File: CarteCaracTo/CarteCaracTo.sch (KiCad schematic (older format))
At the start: 23 parts, among them J2 Conn_01x01, J3 Conn_Coaxial, J4 Conn_Coaxial, J5 Conn_Coaxial, J50 Sub-D50_F, J51 DB15_Male_MountingHoles, J52 DB25_Female_MountingHoles, J6 Conn_Coaxial, J7 Conn_Coaxial, J8 Conn_Coaxial, SW1 SW_3PDT, SW2 SW_DIP_x05, SW3 SW_Slide_DP3T, SW4 SW_SPDT, SW5 SW_SPDT, SW6 SW_SPDT, SW7 SW_3PDT

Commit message: mineur
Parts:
- added U1: OPA4376, Package_SO:SOIC-14_3.9x8.7mm_P1.27mm, symbol Amplifier_Operational:OPA4376
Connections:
- net labels added: +12v
- wire segments 382 -> 398
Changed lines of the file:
@@
 Wire Wire Line
 	1700 10850 1700 10750
+$Comp
+L Amplifier_Operational:OPA4376 U1
+U 5 1 6238513D
+P 7100 10275
+F 0 "U1" H 7058 10321 50  0000 L CNN
+F 1 "OPA4376" H 7058 10230 50  0000 L CNN
+F 2 "Package_SO:SOIC-14_3.9x8.7mm_P1.27mm" H 7050 10375 50  0001 C CNN
+F 3 "http://www.ti.com/lit/ds/symlink/opa376.pdf" H 7150 10475 50  0001 C CNN
+	5    7100 10275
+	1    0    0    -1
+$EndComp
+$Comp
+L Amplifier_Operational:OPA4376 U1
+U 4 1 623861C7
+P 6200 10275
+F 0 "U1" H 6200 10642 50  0000 C CNN
+F 1 "OPA4376" H 6200 10551 50  0000 C CNN
+F 2 "Package_SO:SOIC-14_3.9x8.7mm_P1.27mm" H 6150 10375 50  0001 C CNN
+F 3 "http://www.ti.com/lit/ds/symlink/opa376.pdf" H 6250 10475 50  0001 C CNN
+	4    6200 10275
+	1    0    0    -1
+$EndComp
+$Comp
+L power:GND #PWR0101
+U 1 1 623980F1
+P 7000 10675
+F 0 "#PWR0101" H 7000 10425 50  0001 C CNN
+F 1 "GND" H 7005 10502 50  0000 C CNN
+F 2 "" H 7000 10675 50  0001 C CNN
+F 3 "" H 7000 10675 50  0001 C CNN
+	1    7000 10675
+	1    0    0    -1
+$EndComp
+Wire Wire Line
+	7000 10675 7000 10625
+Wire Wire Line
+	7000 9975 7000 9900
+Wire Wire Line
+	7000 9900 7100 9900
+Text Label 7100 9900 0    50   ~ 0
++12v
+Wire Wire Line
+	13575 1600 13350 1600
+Text Label 13350 1600 2    50   ~ 0
++12v
+Wire Wire Line
+	5900 10175 5550 10175
+Wire Wire Line
+	5550 10175 5550 10575
+Wire Wire Line
+	5900 10375 5775 10375
+Wire Wire Line
+	5775 10375 5775 10575
+Wire Wire Line
+	6500 10275 6525 10275
+Wire Wire Line
+	6525 10275 6525 10575
+Wire Wire Line
+	5550 10575 5775 10575
+Wire Wire Line
+	6900 10575 6900 10625
+Wire Wire Line
+	6900 10625 7000 10625
+Connection ~ 5775 10575
+Wire Wire Line
+	5775 10575 6525 10575
+Connection ~ 7000 10625
+Wire Wire Line
+	7000 10625 7000 10575
+Connection ~ 6525 10575
+Wire Wire Line
+	6525 10575 6900 10575
 $EndSCHEMATC

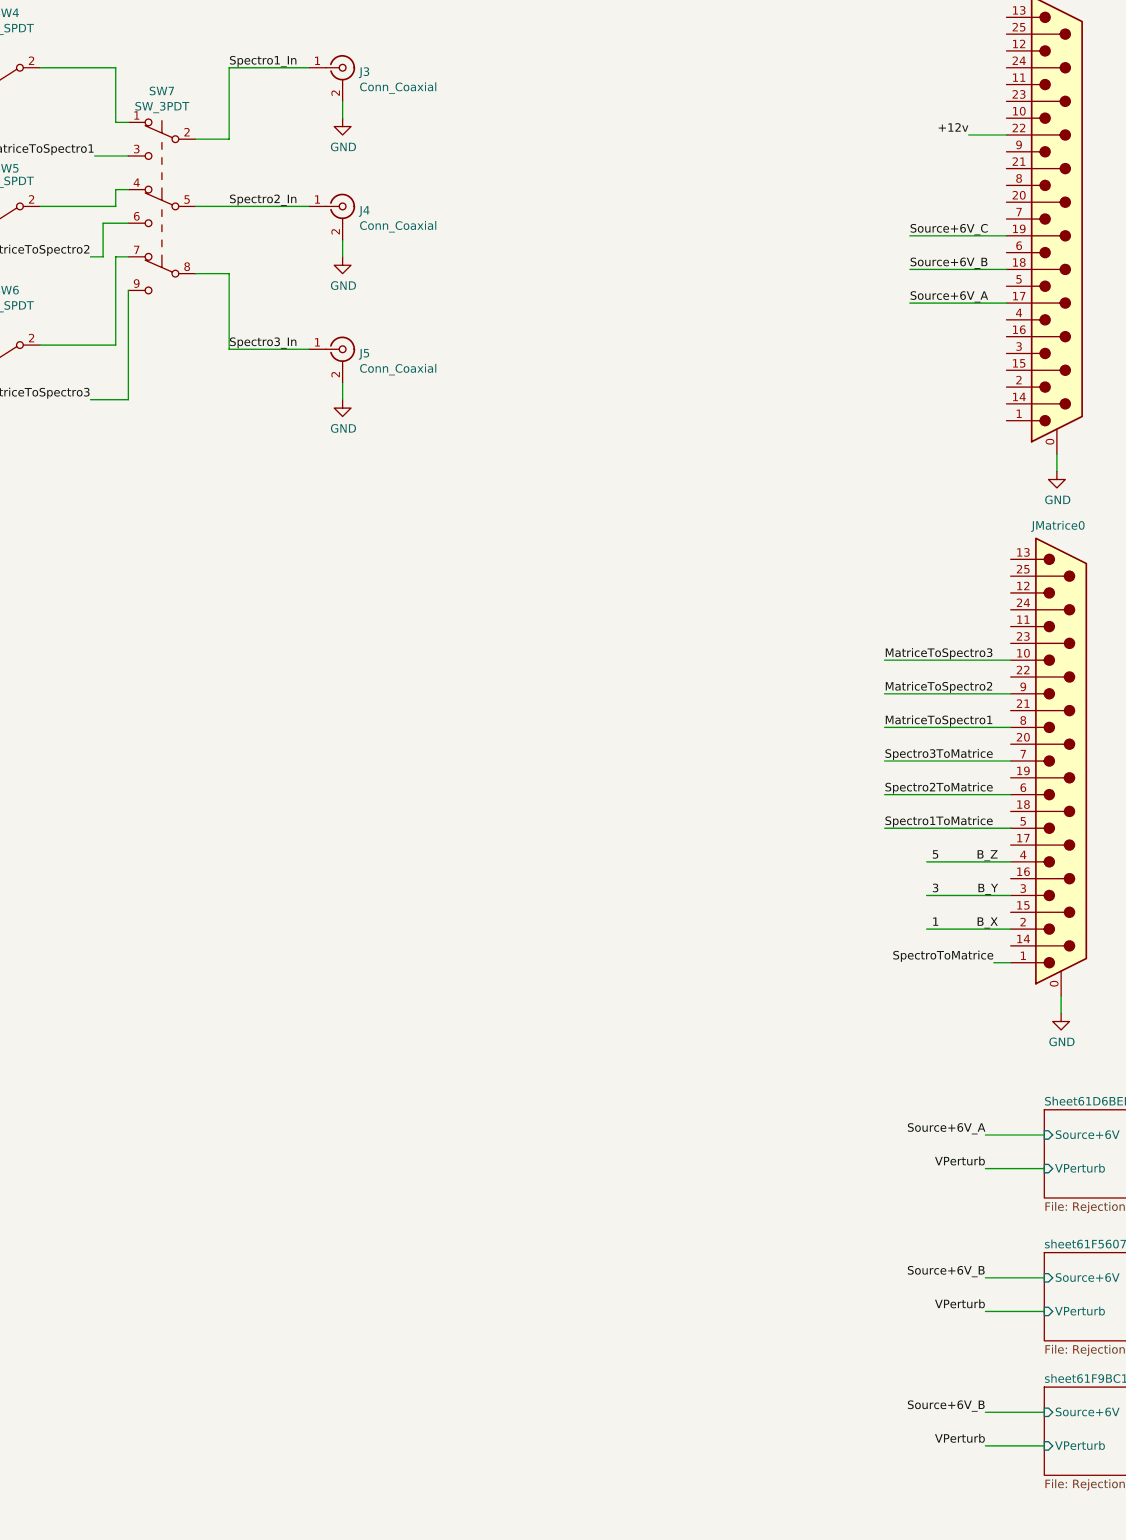
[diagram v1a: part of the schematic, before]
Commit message: Mise en forme de la carte + version carte ASIC et Carac separées
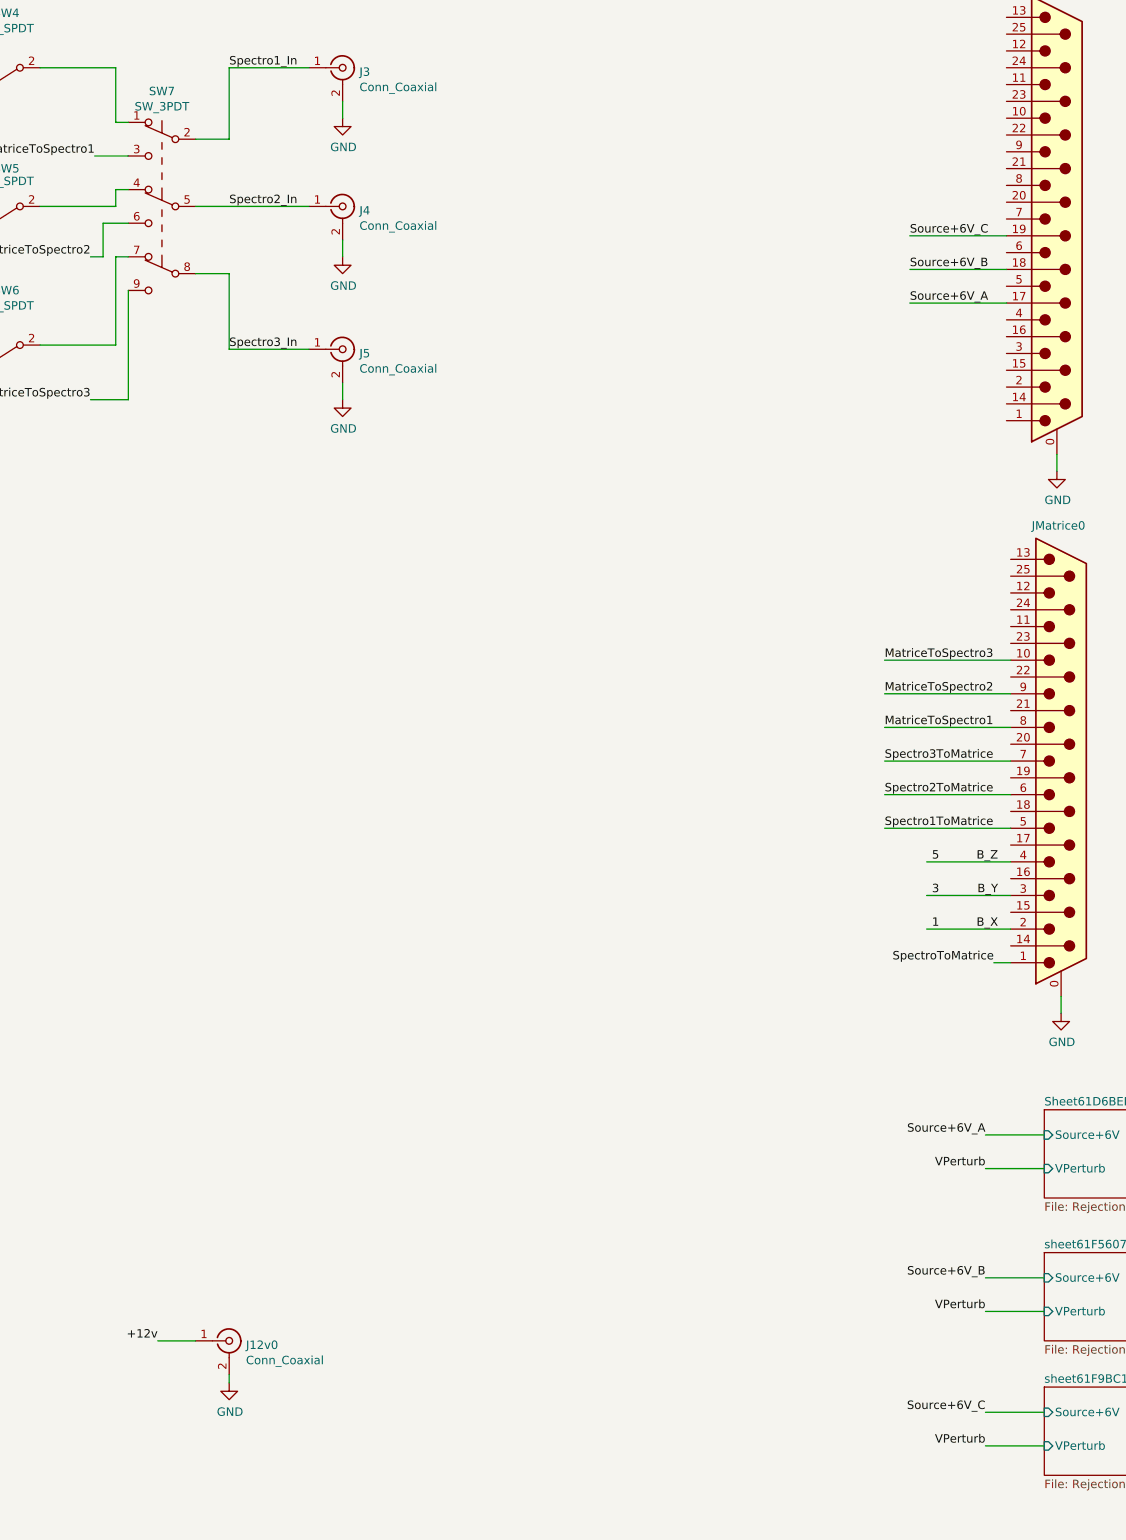
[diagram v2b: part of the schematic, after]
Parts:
- added J12v0: Conn_Coaxial, Connector_Coaxial:SMB_Jack_Vertical, symbol Connector:Conn_Coaxial
- JGSE0, JMatrice0: footprint LibPersoNadj:DCCM25PCBRPN -> Connector_Dsub:DSUB-25_Male_Horizontal_P2.77x2.84mm_EdgePinOffset9.90mm_Housed_MountingHolesOffset11.32mm
- SW7: footprint LibPersoNadj:Switch_DP3T_Slide_MHS233K -> LibPersoNadj:SW_3PDT_M2032TNW01_NKK
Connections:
- wire segments 398 -> 399
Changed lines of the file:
@@
 F 0 "JGSE0" H 13750 3500 50  0000 L CNN
 F 1 "DB25_Male_MountingHoles" H 14055 2011 50  0001 L CNN
-F 2 "LibPersoNadj:DCCM25PCBRPN" H 13875 2100 50  0001 C CNN
+F 2 "Connector_Dsub:DSUB-25_Male_Horizontal_P2.77x2.84mm_EdgePinOffset9.90mm_Housed_MountingHolesOffset11.32mm" H 13875 2100 50  0001 C CNN
 F 3 " ~" H 13875 2100 50  0001 C CNN
 	1    13875 2100
@@
 F 0 "JMatrice0" H 13725 6725 50  0000 L CNN
 F 1 "DB25_Male_MountingHoles" H 14080 5236 50  0001 L CNN
-F 2 "LibPersoNadj:DCCM25PCBRPN" H 13900 5325 50  0001 C CNN
+F 2 "Connector_Dsub:DSUB-25_Male_Horizontal_P2.77x2.84mm_EdgePinOffset9.90mm_Housed_MountingHolesOffset11.32mm" H 13900 5325 50  0001 C CNN
 F 3 " ~" H 13900 5325 50  0001 C CNN
 	1    13900 5325
@@
 F 0 "SW7" H 8550 2710 50  0000 C CNN
 F 1 "SW_3PDT" H 8550 2619 50  0000 C CNN
-F 2 "LibPersoNadj:Switch_DP3T_Slide_MHS233K" H 8550 2425 50  0001 C CNN
+F 2 "LibPersoNadj:SW_3PDT_M2032TNW01_NKK" H 8550 2425 50  0001 C CNN
 F 3 "~" H 8550 2425 50  0001 C CNN
 	1    8550 2025
@@
 	13800 9400 13450 9400
 Text Label 13450 9200 2    50   ~ 0
-Source+6V_B
+Source+6V_C
 Text Label 15125 9300 0    50   ~ 0
 +6V_B
@@
 +12v
 Wire Wire Line
-	13575 1600 13350 1600
-Text Label 13350 1600 2    50   ~ 0
+	8750 8775 8525 8775
+Text Label 8525 8775 2    50   ~ 0
 +12v
 Wire Wire Line
@@
 Wire Wire Line
 	6525 10575 6900 10575
+$Comp
+L Connector:Conn_Coaxial J12v0
+U 1 1 5E2F4810
+P 8950 8775
+F 0 "J12v0" H 9050 8750 50  0000 L CNN
+F 1 "Conn_Coaxial" H 9050 8659 50  0000 L CNN
+F 2 "Connector_Coaxial:SMB_Jack_Vertical" H 8950 8775 50  0001 C CNN
+F 3 " ~" H 8950 8775 50  0001 C CNN
+	1    8950 8775
+	1    0    0    -1
+$EndComp
+$Comp
+L power:GND #PWR0102
+U 1 1 5E3490FC
+P 8950 9025
+F 0 "#PWR0102" H 8950 8775 50  0001 C CNN
+F 1 "GND" H 8955 8852 50  0000 C CNN
+F 2 "" H 8950 9025 50  0001 C CNN
+F 3 "" H 8950 9025 50  0001 C CNN
+	1    8950 9025
+	1    0    0    -1
+$EndComp
+Wire Wire Line
+	8950 9025 8950 8975
 $EndSCHEMATC

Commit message: ID des pins, option capa sur sortie, option GND ou plan de masse sur BNC
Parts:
- removed J2: Conn_01x01, Connector_Coaxial:BNC_Amphenol_B6252HB-NPP3G-50_Horizontal, symbol Connector_Generic:Conn_01x01
- added C1, C2, C3: C, Capacitor_SMD:C_0805_2012Metric_Pad1.15x1.40mm_HandSolder, symbol Device:C
- added JDec_SA1, JDec_SA2, JDec_SA3, JGND_I_SA1, JGND_I_SA2, JGND_I_SA3, JGND_O_SA1, JGND_O_SA2, JGND_O_SA3: Conn_01x03, Connector_PinHeader_2.54mm:PinHeader_1x03_P2.54mm_Vertical, symbol Connector_Generic:Conn_01x03
- added JMasse0: Conn_01x02, Connector_PinHeader_2.54mm:PinHeader_1x02_P2.54mm_Vertical, symbol Connector_Generic:Conn_01x02
- added J_12v0, J_I_SA1, J_I_SA2, J_I_SA3, J_O_SA1, J_O_SA2, J_O_SA3, J_Perturb1: Conn_01x01, Connector_PinHeader_2.54mm:PinHeader_1x01_P2.54mm_Vertical, symbol Connector_Generic:Conn_01x01
- added J_Perturb0: Conn_Coaxial, Connector_Coaxial:BNC_Amphenol_B6252HB-NPP3G-50_Horizontal, symbol Connector:Conn_Coaxial
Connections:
- net labels added: CAL, CAL_RTN, CAL_Shield, CR_X, CR_Y, CR_Z, Chassis, GNDREF, In2P_X, In2P_Y, In2P_Z, M_X, M_Y, M_Z, PWR_Shield_A, PWR_Shield_B, PWR_Shield_C, RTN_A, RTN_B, RTN_C, RTN_Mon_A, RTN_Mon_B, Sh_X, Sh_Y, Sh_Z, Temp_Mon_A, Temp_Mon_B, VDD_X, VDD_Y, VDD_Z, V_BIAS_LNA_X, V_BIAS_LNA_Y, V_BIAS_LNA_Z, XShield, YShield, ZShield
- net labels removed: SpectroToMatrice
- wire segments 399 -> 548
- no-connect marks 1 -> 10
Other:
- moved on the sheet: J12v0, J3, J4, J5, J50, J6, J7, J8, SW3, SW4, SW5, SW6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

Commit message: v0 near finished
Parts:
- added TPGND0, TPV0: TestPoint, LibPersoNadj:Banana_test_point_4mm, symbol Connector:TestPoint
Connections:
- wire segments 548 -> 550
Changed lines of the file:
@@
 Wire Wire Line
 	700  4275 1400 4275
-Text Label 2525 4875 0    50   ~ 0
-Sy
-Wire Wire Line
-	2300 4875 2750 4875
 Text Label 700  4375 0    50   ~ 0
 Sz
@@
 Wire Wire Line
 	550  3075 1400 3075
-Text Label 2725 4375 2    50   ~ 0
-RTNz
 Text Label 700  4975 0    50   ~ 0
 RTNy
-Text Label 2725 4175 2    50   ~ 0
-RTNx
-Wire Wire Line
-	2300 4175 2725 4175
 Wire Wire Line
 	700  4975 1400 4975
-Wire Wire Line
-	2300 4375 2725 4375
-Text Label 2725 5275 2    50   ~ 0
-+6V_C
-Text Label 2525 4575 0    50   ~ 0
-+6V_B
 Text Label 700  5175 0    50   ~ 0
 +6V_A
 Wire Wire Line
 	700  5175 1400 5175
-Wire Wire Line
-	2300 4575 2725 4575
-Wire Wire Line
-	2300 5275 2725 5275
 Wire Wire Line
 	4850 10325 4775 10325
@@
 L power:GNDREF #PWR0103
 U 1 1 5E4731B1
-P 7175 8225
-F 0 "#PWR0103" H 7175 7975 50  0001 C CNN
-F 1 "GNDREF" H 7180 8052 50  0000 C CNN
-F 2 "" H 7175 8225 50  0001 C CNN
-F 3 "" H 7175 8225 50  0001 C CNN
-	1    7175 8225
-	1    0    0    -1
-$EndComp
-Wire Wire Line
-	7175 8225 7175 7975
+P 7175 8400
+F 0 "#PWR0103" H 7175 8150 50  0001 C CNN
+F 1 "GNDREF" H 7180 8227 50  0000 C CNN
+F 2 "" H 7175 8400 50  0001 C CNN
+F 3 "" H 7175 8400 50  0001 C CNN
+	1    7175 8400
+	1    0    0    -1
+$EndComp
+Wire Wire Line
+	7175 8400 7175 8125
 $Comp
 L power:GNDREF #PWR0106
@@
 	0    -1   -1   0
 $EndComp
-Wire Wire Line
-	2850 3375 2850 3475
-Wire Wire Line
-	2850 5625 1850 5625
-Wire Wire Line
-	2300 3375 2850 3375
 Connection ~ 1850 5625
 Wire Wire Line
 	1850 5625 1850 5575
-Wire Wire Line
-	2300 3475 2850 3475
-Connection ~ 2850 3475
-Wire Wire Line
-	2850 3475 2850 3575
-Wire Wire Line
-	2300 3575 2850 3575
-Connection ~ 2850 3575
-Wire Wire Line
-	2850 3575 2850 4275
-Wire Wire Line
-	2300 4275 2850 4275
-Connection ~ 2850 4275
-Wire Wire Line
-	2850 4275 2850 4675
-Wire Wire Line
-	2300 4675 2850 4675
-Connection ~ 2850 4675
-Wire Wire Line
-	2850 4675 2850 4775
-Wire Wire Line
-	2300 4775 2850 4775
-Connection ~ 2850 4775
-Wire Wire Line
-	2850 4775 2850 4975
-Wire Wire Line
-	2300 4975 2850 4975
-Connection ~ 2850 4975
-Wire Wire Line
-	2300 5175 2850 5175
-Wire Wire Line
-	2850 4975 2850 5175
-Connection ~ 2850 5175
-Wire Wire Line
-	2850 5175 2850 5375
-Wire Wire Line
-	2300 5375 2850 5375
-Connection ~ 2850 5375
-Wire Wire Line
-	2850 5375 2850 5625
 $Comp
 L Connector_Generic:Conn_01x02 JMasse0
@@
 L power:GND #PWR0111
 U 1 1 5EEACD10
-P 7075 8025
-F 0 "#PWR0111" H 7075 7775 50  0001 C CNN
-F 1 "GND" H 7080 7852 50  0000 C CNN
-F 2 "" H 7075 8025 50  0001 C CNN
-F 3 "" H 7075 8025 50  0001 C CNN
-	1    7075 8025
-	1    0    0    -1
-$EndComp
-Wire Wire Line
-	7075 8025 7075 7975
+P 7075 8200
+F 0 "#PWR0111" H 7075 7950 50  0001 C CNN
+F 1 "GND" H 7080 8027 50  0000 C CNN
+F 2 "" H 7075 8200 50  0001 C CNN
+F 3 "" H 7075 8200 50  0001 C CNN
+	1    7075 8200
+	1    0    0    -1
+$EndComp
+Wire Wire Line
+	7075 8200 7075 8125
 $Comp
 L Connector_Generic:Conn_01x01 J_O_SA1
@@
 Wire Wire Line
 	13575 3300 13025 3300
-Text Label 2525 2975 0    50   ~ 0
-CR_X
-Text Label 2525 3075 0    50   ~ 0
-CR_Y
-Text Label 2525 3175 0    50   ~ 0
-CR_Z
 Text Label 1000 3275 2    50   ~ 0
 Temp_Mon_A
 Text Label 625  3675 0    50   ~ 0
 Chassis
-Text Label 2525 3675 0    50   ~ 0
-In2P_X
 Text Label 700  3775 0    50   ~ 0
 In2P_Y
-Text Label 2525 4475 0    50   ~ 0
-RTN_Mon_B
-Text Label 2525 4775 0    50   ~ 0
-CAL_RTN
-Text Label 2525 4975 0    50   ~ 0
-ZShield
-Text Label 2525 5175 0    50   ~ 0
-RTN_A
-Text Label 2525 5375 0    50   ~ 0
-CAL_Shield
 Text Label 675  4575 0    50   ~ 0
 PWR_Shield_A
@@
 Text Label 675  5375 0    50   ~ 0
 RTN_C
-Text Label 2525 3375 0    50   ~ 0
-Sh_X
 Text Label 625  3375 0    50   ~ 0
 M_X
-Text Label 2525 3275 0    50   ~ 0
-RTN_Mon_A
-Text Label 2525 3475 0    50   ~ 0
-Sh_Y
 Text Label 625  3475 0    50   ~ 0
 M_Y
-Text Label 2525 3575 0    50   ~ 0
-Sh_Z
 Text Label 625  3575 0    50   ~ 0
 M_Z
 Wire Wire Line
-	2300 2975 2750 2975
-Wire Wire Line
-	2300 3075 2750 3075
-Wire Wire Line
-	2300 3175 2750 3175
-Wire Wire Line
 	550  3275 1400 3275
 Wire Wire Line
-	2300 3275 2975 3275
-Wire Wire Line
 	550  3375 1400 3375
 Wire Wire Line
@@
 Wire Wire Line
 	550  3575 1400 3575
-Text Label 2525 3775 0    50   ~ 0
-In2P_Z
-Text Label 2525 4275 0    50   ~ 0
-YShield
-Text Label 2525 4675 0    50   ~ 0
-PWR_Shield_C
-Text Label 2525 5075 0    50   ~ 0
-Temp_Mon_B
 Text Label 675  4475 0    50   ~ 0
 RTN_Mon_A
@@
 PWR_Shield_B
 Wire Wire Line
-	2300 3775 2750 3775
-Wire Wire Line
-	2300 3675 2750 3675
-Wire Wire Line
 	625  3775 1400 3775
-Wire Wire Line
-	2300 5075 2750 5075
-Wire Wire Line
-	2300 4475 2750 4475
 Wire Wire Line
 	675  4775 1400 4775
@@
 Wire Wire Line
 	575  5625 575  6225
-Text Label 2525 3875 0    50   ~ 0
-V_BIAS_LNA_Y
-Wire Wire Line
-	2300 3875 2750 3875
 Wire Wire Line
 	13575 1100 13025 1100
@@
 Text Label 2350 3975 0    50   ~ 0
 22
-Wire Wire Line
-	2300 3975 2750 3975
-Wire Wire Line
-	2300 4075 2750 4075
 Text Label 2350 4075 0    50   ~ 0
 24
+Text Label 700  4075 0    50   ~ 0
+VDD_Y
+Wire Wire Line
+	5050 10525 5050 10725
+Text Label 2525 4075 0    50   ~ 0
+VDD_Z
 Text Label 2525 3975 0    50   ~ 0
 VDD_X
-Text Label 2525 4075 0    50   ~ 0
-VDD_Z
-Text Label 700  4075 0    50   ~ 0
-VDD_Y
-Wire Wire Line
-	5050 10525 5050 10725
+Wire Wire Line
+	2300 4075 2750 4075
+Wire Wire Line
+	2300 3975 2750 3975
+Wire Wire Line
+	2300 3875 2750 3875
+Text Label 2525 3875 0    50   ~ 0
+V_BIAS_LNA_Y
+Wire Wire Line
+	2300 4475 2750 4475
+Wire Wire Line
+	2300 5075 2750 5075
+Wire Wire Line
+	2300 3675 2750 3675
+Wire Wire Line
+	2300 3775 2750 3775
+Text Label 2525 5075 0    50   ~ 0
+Temp_Mon_B
+Text Label 2525 4675 0    50   ~ 0
+PWR_Shield_C
+Text Label 2525 4275 0    50   ~ 0
+YShield
+Text Label 2525 3775 0    50   ~ 0
+In2P_Z
+Wire Wire Line
+	2300 3275 2975 3275
+Wire Wire Line
+	2300 3175 2975 3175
+Wire Wire Line
+	2300 3075 2975 3075
+Wire Wire Line
+	2300 2975 2975 2975
+Text Label 2525 3575 0    50   ~ 0
+Sh_Z
+Text Label 2525 3475 0    50   ~ 0
+Sh_Y
+Text Label 2525 3275 0    50   ~ 0
+RTN_Mon_A
+Text Label 2525 3375 0    50   ~ 0
+Sh_X
+Text Label 2525 5375 0    50   ~ 0
+CAL_Shield
+Text Label 2525 5175 0    50   ~ 0
+RTN_A
+Text Label 2525 4975 0    50   ~ 0
+ZShield
+Text Label 2525 4775 0    50   ~ 0
+CAL_RTN
+Text Label 2525 4475 0    50   ~ 0
+RTN_Mon_B
+Text Label 2525 3675 0    50   ~ 0
+In2P_X
+Text Label 2525 3175 0    50   ~ 0
+CR_Z
+Text Label 2525 3075 0    50   ~ 0
+CR_Y
+Text Label 2525 2975 0    50   ~ 0
+CR_X
+Wire Wire Line
+	3125 5375 3125 5625
+Connection ~ 3125 5375
+Wire Wire Line
+	2300 5375 3125 5375
+Wire Wire Line
+	3125 5175 3125 5375
+Connection ~ 3125 5175
+Wire Wire Line
+	3125 4975 3125 5175
+Wire Wire Line
+	2300 5175 3125 5175
+Connection ~ 3125 4975
+Wire Wire Line
+	2300 4975 3125 4975
+Wire Wire Line
+	3125 4775 3125 4975
+Connection ~ 3125 4775
+Wire Wire Line
+	2300 4775 3125 4775
+Wire Wire Line
+	3125 4675 3125 4775
+Connection ~ 3125 4675
+Wire Wire Line
+	2300 4675 3125 4675
+Wire Wire Line
+	3125 4275 3125 4675
+Connection ~ 3125 4275
+Wire Wire Line
+	2300 4275 3125 4275
+Wire Wire Line
+	3125 3575 3125 4275
+Connection ~ 3125 3575
+Wire Wire Line
+	2300 3575 3125 3575
+Wire Wire Line
+	3125 3475 3125 3575
+Connection ~ 3125 3475
+Wire Wire Line
+	2300 3475 3125 3475
+Wire Wire Line
+	2300 3375 3125 3375
+Wire Wire Line
+	3125 5625 1850 5625
+Wire Wire Line
+	3125 3375 3125 3475
+Wire Wire Line
+	2300 5275 2725 5275
+Wire Wire Line
+	2300 4575 2725 4575
+Text Label 2525 4575 0    50   ~ 0
++6V_B
+Text Label 2525 5275 0    50   ~ 0
++6V_C
+Wire Wire Line
+	2300 4375 2725 4375
+Wire Wire Line
+	2300 4175 2725 4175
+Text Label 2725 4175 2    50   ~ 0
+RTNx
+Text Label 2725 4375 2    50   ~ 0
+RTNz
+Wire Wire Line
+	2300 4875 2750 4875
+Text Label 2525 4875 0    50   ~ 0
+Sy
+$Comp
+L Connector:TestPoint TPGND0
+U 1 1 5E1EBC83
+P 7075 8125
+F 0 "TPGND0" V 7100 8500 50  0000 C CNN
+F 1 "TestPoint" V 7025 8500 50  0000 C CNN
+F 2 "LibPersoNadj:Banana_test_point_4mm" H 7275 8125 50  0001 C CNN
+F 3 "~" H 7275 8125 50  0001 C CNN
+	1    7075 8125
+	0    -1   -1   0
+$EndComp
+Connection ~ 7075 8125
+Wire Wire Line
+	7075 8125 7075 7975
+$Comp
+L Connector:TestPoint TPV0
+U 1 1 5E26F249
+P 7175 8125
+F 0 "TPV0" V 7129 8313 50  0000 L CNN
+F 1 "TestPoint" V 7220 8313 50  0000 L CNN
+F 2 "LibPersoNadj:Banana_test_point_4mm" H 7375 8125 50  0001 C CNN
+F 3 "~" H 7375 8125 50  0001 C CNN
+	1    7175 8125
+	0    1    1    0
+$EndComp
+Connection ~ 7175 8125
+Wire Wire Line
+	7175 8125 7175 7975
 $EndSCHEMATC
